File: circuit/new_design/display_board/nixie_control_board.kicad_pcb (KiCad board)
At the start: 4 copper layers, 200 x 63 mm, 14 parts, among them P1 CONN_02X03, P5 CONN_01X08, P6 CONN_01X12, SW1 SW_PUSH, SW2 SW_PUSH, SW3 SW_PUSH, U10 IN-14, U11 IN-14, U12 IN-14, U13 IN-14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

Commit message: Finish the new display board
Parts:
- added REF**: Symbol_HighVoltage_Type2_CopperTop_VerySmall, warning:warning, B.Cu at (67.7, 82.5)
- added REF**: MountingHole_2.2mm_M2, Mounting_Holes:MountingHole_2.2mm_M2, F.Cu at (152.1, 74.6)
- added REF**: MountingHole_2.2mm_M2, Mounting_Holes:MountingHole_2.2mm_M2, F.Cu at (152.1, 129.6)
- added REF**: MountingHole_2.2mm_M2, Mounting_Holes:MountingHole_2.2mm_M2, F.Cu at (248.1, 129.6)
- added REF**: MountingHole_2.2mm_M2, Mounting_Holes:MountingHole_2.2mm_M2, F.Cu at (248.1, 74.6)
- added REF**: MountingHole_2.2mm_M2, Mounting_Holes:MountingHole_2.2mm_M2, F.Cu at (56.1, 129.6)
- added REF**: MountingHole_2.2mm_M2, Mounting_Holes:MountingHole_2.2mm_M2, F.Cu at (56.1, 74.6)
- added REF**: Symbol_HighVoltage_Type2_CopperTop_VerySmall, warning:warning, F.Cu at (67.2, 122.1)
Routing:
- net cathode_comma_right: track 283.4 -> 292.9 mm
- net cathode1: track 290.7 -> 288.7 mm
- net anode7: track 82.8 -> 81.1 mm
- net cathode7: track 413.1 -> 413.2 mm, vias 8 -> 9
- added copper zone on B.Cu, net (none)
- added copper zone on F.Cu, net (none)
- added copper zone on In1.Cu, net (none)
- added copper zone on In2.Cu, net (none)

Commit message: Finish new version hardware design
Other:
- rule trace_min: 0.2 -> 0.25
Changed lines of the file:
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@@
   )
   (setup
-    (last_trace_width 0.7)
+    (last_trace_width 0.25)
     (user_trace_width 0.55)
     (user_trace_width 0.6)
@@
     (zone_clearance 0.508)
     (zone_45_only yes)
-    (trace_min 0.2)
+    (trace_min 0.25)
     (segment_width 0.15)
     (edge_width 0.15)
@@
     (visible_elements FFFFFF7F)
     (pcbplotparams
-      (layerselection 0x01030_80000001)
+      (layerselection 0x01030_80000007)
       (usegerberextensions true)
       (excludeedgelayer true)

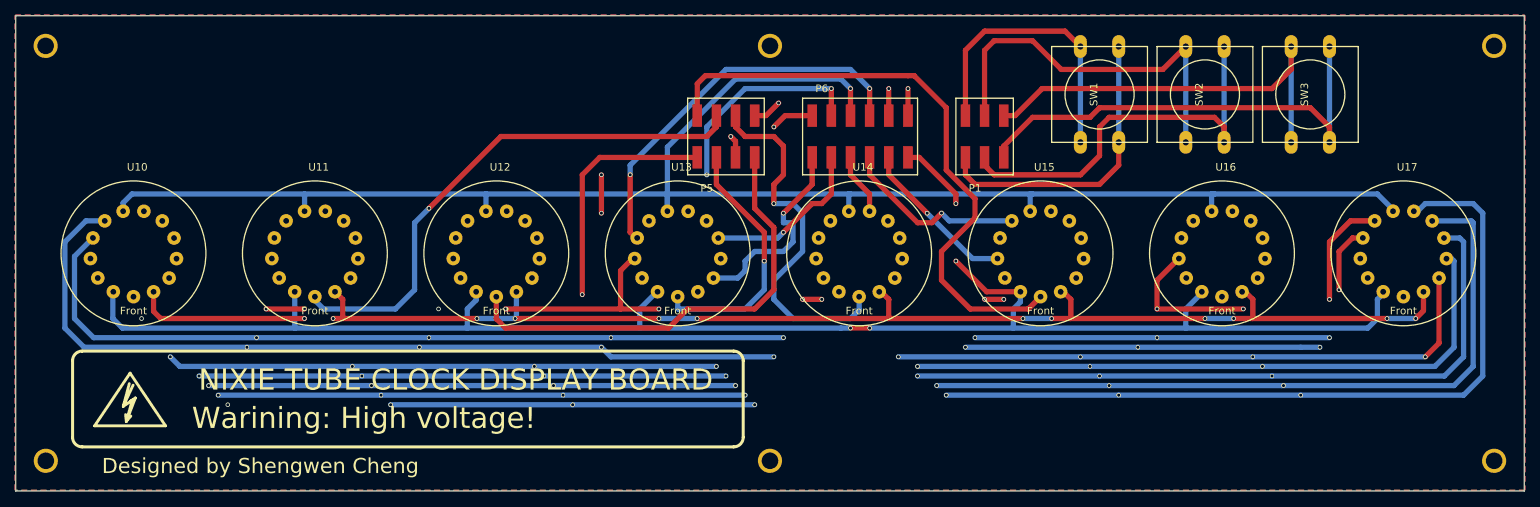
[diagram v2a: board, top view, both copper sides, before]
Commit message: Eliminate display borads layer
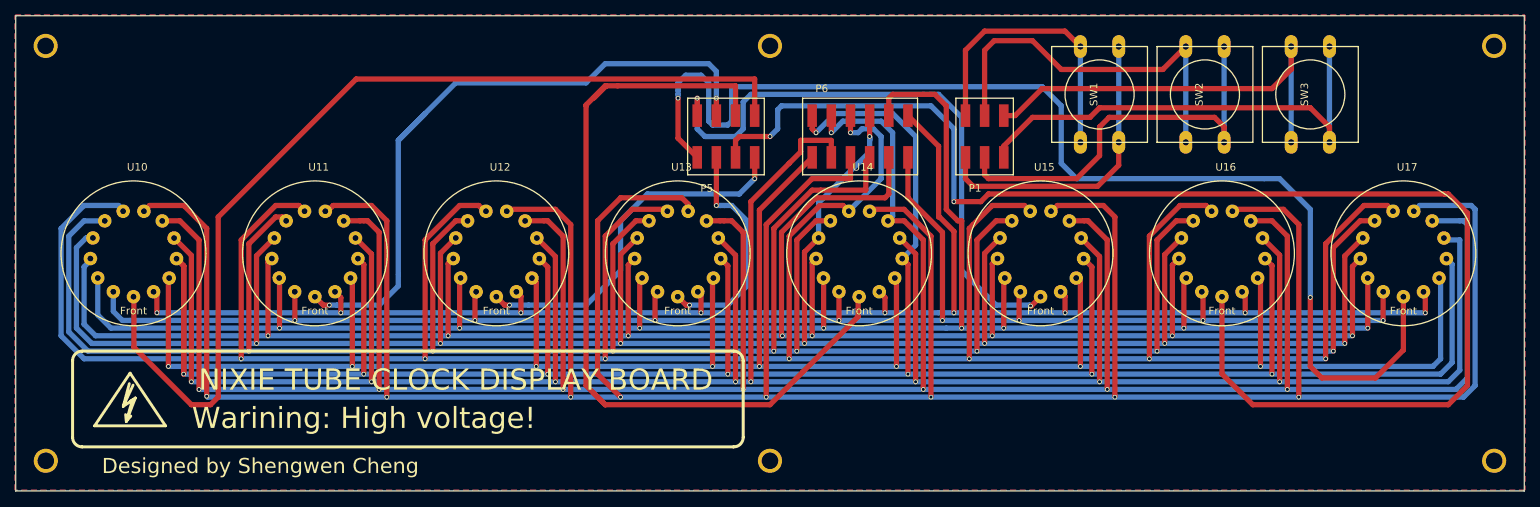
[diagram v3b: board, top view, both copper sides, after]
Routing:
- net cathode5: track 226.5 -> 396.8 mm, vias 1 -> 8
- net anode4: track 96.7 -> 183.5 mm, vias 1 -> 2
- net cathode_comma_right: track 292.9 -> 220.9 mm, vias 13 -> 9
- net anode3: track 49.0 -> 112.0 mm, vias 1 -> 0
- net cathode2: track 251.1 -> 286.7 mm, vias 13 -> 8
- net cathode3: track 338.4 -> 306.9 mm, vias 10 -> 8
- net cathode6: track 446.5 -> 473.9 mm, vias 7 -> 8
- net cathode1: track 288.7 -> 262.3 mm, vias 3 -> 8
- net cathode9: track 318.8 -> 343.4 mm
- net anode1: track 105.6 -> 128.9 mm, vias 1 -> 0
- net anode5: track 70.9 -> 91.6 mm, vias 1 -> 2
- net cathode8: track 354.9 -> 369.3 mm
- net cathode7: track 413.2 -> 399.5 mm, vias 9 -> 8
- net cathode_comma_left: track 236.0 -> 222.5 mm, vias 4 -> 8
- net anode2: track 60.9 -> 48.3 mm, vias 0 -> 2
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- removed copper zone on In1.Cu, net (none)
- removed copper zone on In2.Cu, net (none)
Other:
- copper layers 4 -> 2
